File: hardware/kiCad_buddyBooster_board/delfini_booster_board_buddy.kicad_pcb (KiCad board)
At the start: 2 copper layers, 150 parts, among them J1 Screw_Terminal_1x04, J2 Screw_Terminal_1x04, J3 Screw_Terminal_1x04, J4 Screw_Terminal_1x04, J5 1792229, J6 1792229, J7 Screw_Terminal_1x04, J8 1792229, J9 1792229, P1 CONN_01X03, P11 CONN_01X03, P12 CONN_01X03, P13 CONN_01X03, P14 CONN_01X02, P15 CONN_01X03, P16 CONN_01X02, P17 CONN_01X02, P18 CONN_01X03, P19 CONN_01X03, P2 CONN_01X05, P20 CONN_01X03, P21 CONN_01X03, P22 CONN_01X01, P23 CONN_01X01, P24 CONN_01X01, P25 CONN_01X03, P26 CONN_01X01, P27 CONN_01X01, P28 CONN_01X01, P29 CONN_01X03, P3 CONN_01X05, P30 CONN_01X03, P31 CONN_01X03, P32 CONN_01X01, P33 CONN_01X04, P34 CONN_01X04, P4 CONN_02X10, P5 CONN_02X10, P6 CONN_02X10, P7 CONN_02X10, P8 CONN_01X03, P9 CONN_01X03, Q1 2N7002, Q2 2N7002, Q3 2N7002, Q4 2N7002, Q5 IRF9540N, Q6 IRF9540N, Q7 2N7002, U1 TMP275, U2 T90-Relay, U3 tps2112a, U4 LM7812, U5 R-783.3-1.0, U6 T90-Relay, U7 TXB0104

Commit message: -pcb- started routing
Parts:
- moved C20 10.1 mm to (99.1, 95.6), turned to 0 degrees
- moved U1 8.25 mm to (126.4, 103.4), turned to 90 degrees
- moved P18 4.45 mm to (92.2, 108.4)
- moved Q2 4.07 mm to (104.2, 96.4)
- moved R38 3.42 mm to (118.8, 109.1)
- moved Q4 3.42 mm to (111.2, 106.5)
- moved R34 3.24 mm to (104.2, 103.4)
- moved R28 3.24 mm to (99.8, 103.4)
- moved C19 3.24 mm to (99.1, 97.0)
- moved Q7 3.24 mm to (102.9, 106.5)
- moved R37 3.24 mm to (113.7, 109.1)
- moved U3 3.24 mm to (101.0, 100.8)
- moved C29 3.24 mm to (103.6, 109.1)
- moved R27 3.24 mm to (99.8, 104.9)
- moved R29 3.24 mm to (108.8, 98.3)
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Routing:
- net /BAT_PWR_IN: track 0.00 -> 109.1 mm
- net /UART_SABER_TX: track 0.00 -> 106.7 mm, vias 0 -> 2
- net /ULTA1_PULSE_BACK: track 0.00 -> 50.6 mm
- net +5V: track 0.00 -> 50.4 mm
- net /E_BRAKE_IN: track 0.00 -> 50.0 mm
- net /ULTRA0_TRIG_OUT: track 0.00 -> 48.9 mm
- net /ULTRA1_TRIG_OUT: track 0.00 -> 46.3 mm
- net /ULTA0_PULSE_BACK: track 0.00 -> 46.1 mm
- net /MOTOR_BRAKE_EN_N: track 0.00 -> 38.6 mm
- net Net-(Q4-Pad3): track 0.00 -> 37.7 mm
- net Net-(J3-Pad1): track 0.00 -> 23.7 mm
- net Net-(J1-Pad1): track 0.00 -> 13.6 mm
- net Net-(J3-Pad3): track 0.00 -> 11.9 mm
- net /RELAY_COIL: track 0.00 -> 11.7 mm
- net Net-(C21-Pad1): track 0.00 -> 8.81 mm
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- added copper zone on F.Cu, net /BAT_PWR_IN
- added copper zone on F.Cu, net /BAT_PWR_OUT
- added copper zone on F.Cu, net Net-(J6-Pad1)
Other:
- net class 5V added: clearance 0.2, trace_width 1.016, via_dia 0.8, via_drill 0.4

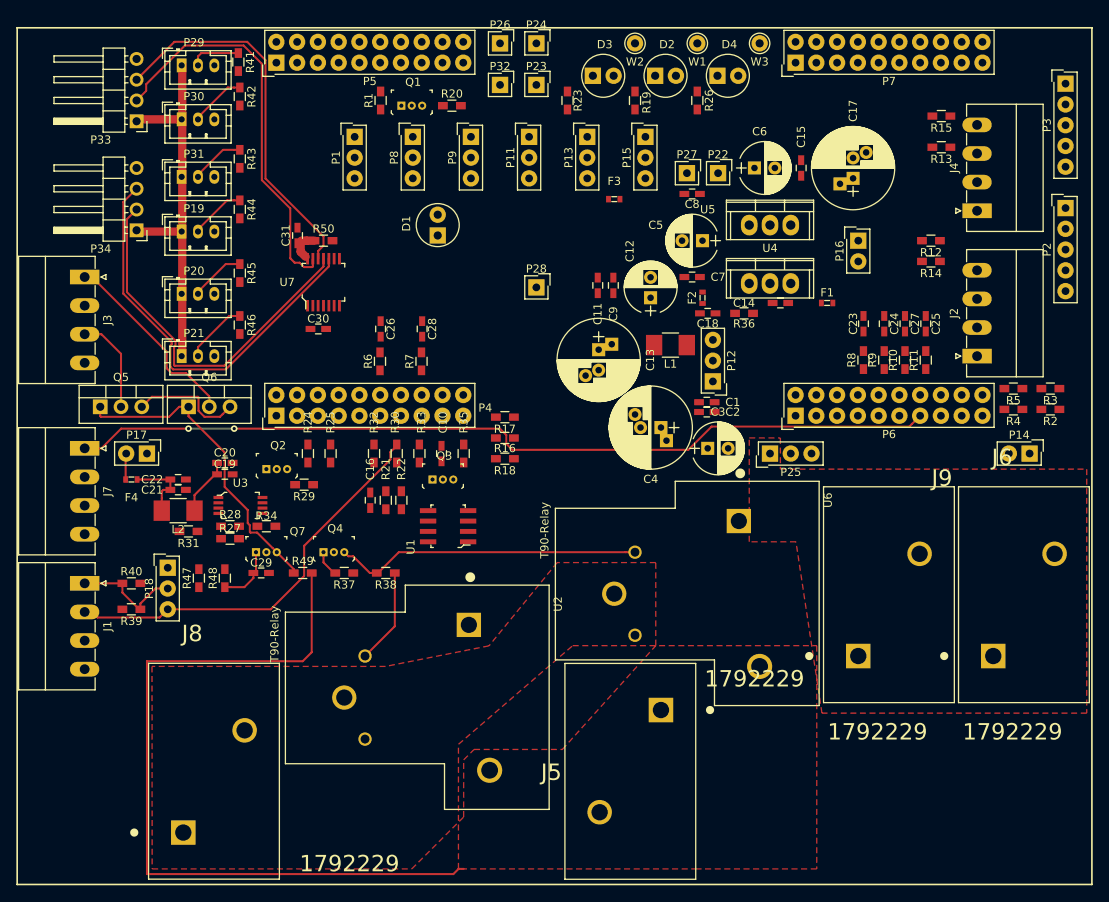
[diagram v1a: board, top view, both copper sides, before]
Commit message: -PCB- Moved Regulators around -PCB- Moved ADC inputs around -Swapped pins around, by grouping
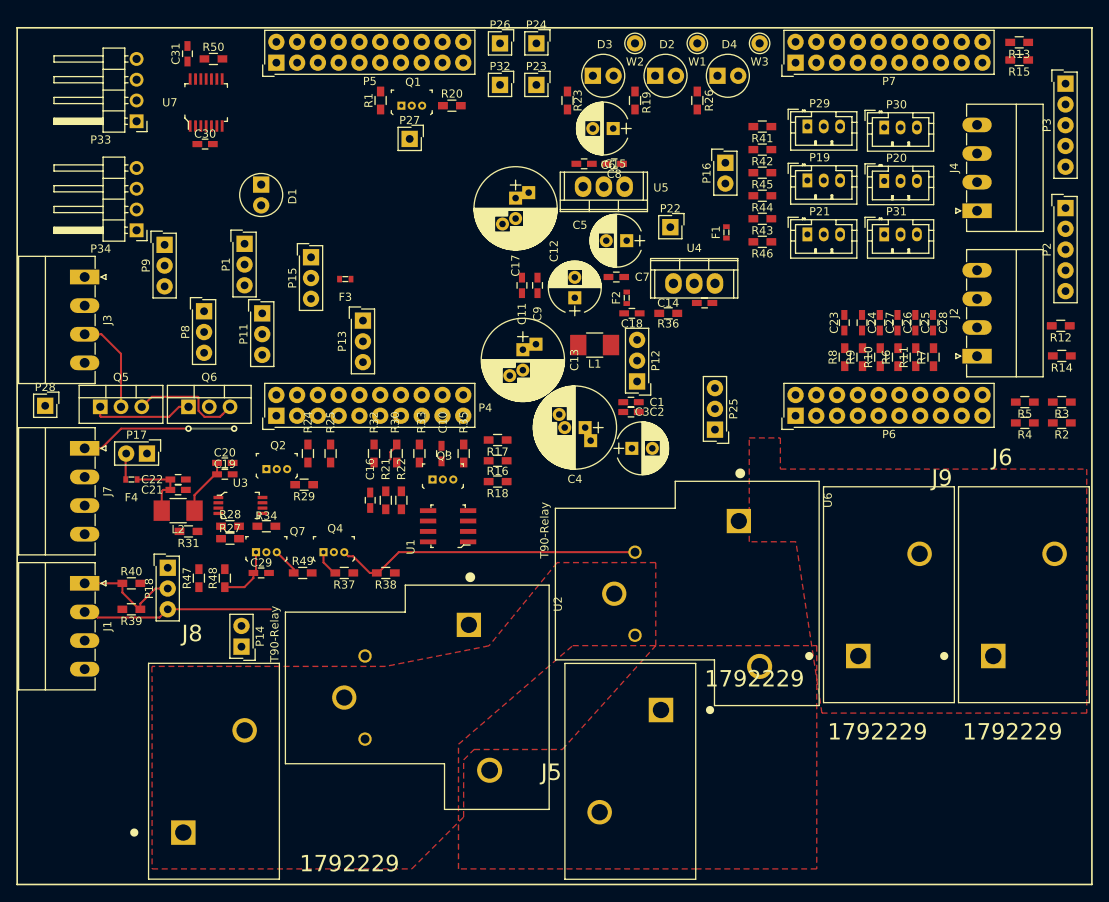
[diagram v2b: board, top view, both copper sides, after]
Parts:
- moved P14 99.2 mm to (101.2, 118.1), turned to 180 degrees
- moved P20 87.0 mm to (179.8, 61.1)
- moved P31 86.2 mm to (179.8, 67.7)
- moved P30 85.9 mm to (179.8, 54.6)
- moved P21 78.0 mm to (170.4, 67.7)
- moved P29 76.9 mm to (170.4, 54.5)
- moved P19 76.8 mm to (170.4, 61.1)
- moved R45 65.1 mm to (164.9, 60.1), turned to 180 degrees
- moved R46 64.7 mm to (164.9, 68.6), turned to 180 degrees
- moved R41 64.6 mm to (164.9, 54.5), turned to 180 degrees
- moved R43 64.3 mm to (164.9, 65.8), turned to 180 degrees
- moved R42 64.2 mm to (164.9, 57.3), turned to 180 degrees
- moved R44 63.9 mm to (164.9, 62.9), turned to 180 degrees
- moved R6 63.4 mm to (181.5, 82.7)
- moved C26 63.2 mm to (181.4, 78.5)
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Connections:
- net /ULTA0_PULSE_BACK renamed /ULTRA0_PULSE_BACK
- net /ULTA1_PULSE_BACK renamed /ULTRA1_PULSE_BACK
- P5 pad 11: Net-(P5-Pad11) -> /ULTRA1_PULSE_BACK_BUFFD
- P5 pad 9: Net-(P5-Pad9) -> /ULTRA0_PULSE_BACK_BUFFD
- P7 pad 1: /ULTA0_PULSE_BACK_BUFFD -> Net-(P7-Pad1)
- P7 pad 3: /ULTA1_PULSE_BACK_BUFFD -> Net-(P7-Pad3)
- R10 pad 1: Net-(P6-Pad16) -> Net-(P6-Pad10)
- R10 pad 2: /ADC4_IN_C2000 -> /ADC2_IN_C2000
- R11 pad 1: Net-(P6-Pad18) -> Net-(P6-Pad14)
- R11 pad 2: /ADC2_IN_C2000 -> /ADC4_IN_C2000
- R6 pad 1: Net-(P4-Pad12) -> Net-(P6-Pad12)
- R7 pad 1: Net-(P4-Pad16) -> Net-(P6-Pad16)
- R8 pad 1: Net-(P6-Pad8) -> Net-(P6-Pad6)
- R9 pad 1: Net-(P6-Pad14) -> Net-(P6-Pad8)
- U7 pad 3: /ULTA0_PULSE_BACK_BUFFD -> /ULTRA0_PULSE_BACK_BUFFD
- U7 pad 5: /ULTA1_PULSE_BACK_BUFFD -> /ULTRA1_PULSE_BACK_BUFFD
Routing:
- net /BAT_PWR_IN: track 109.1 -> 13.8 mm
- net /UART_SABER_TX: track 106.7 -> 19.4 mm
- net /ULTRA1_PULSE_BACK: track 50.6 -> 0.00 mm
- net +5V: track 50.4 -> 0.00 mm
- net /ULTRA0_TRIG_OUT: track 48.9 -> 0.00 mm
- net /ULTRA1_TRIG_OUT: track 46.3 -> 0.00 mm
- net /ULTRA0_PULSE_BACK: track 46.1 -> 0.00 mm
- net /E_BRAKE_IN: track 50.0 -> 25.6 mm
- net Net-(J3-Pad1): track 23.7 -> 0.90 mm
- net /MOTOR_BRAKE_EN_N: track 38.6 -> 15.9 mm
- net /RELAY_COIL: track 11.7 -> 0.00 mm
- net /ADC5_OUTPUT: track 7.79 -> 0.00 mm
- net /ADC1_OUTPUT: track 6.87 -> 0.00 mm
- net /ADC3_OUTPUT: track 6.84 -> 0.00 mm
- net /ADC4_OUTPUT: track 6.77 -> 0.00 mm
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
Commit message: -PCB- End of night commit. Minor tweaks
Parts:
- moved R1 24.4 mm to (96.5, 62.3)
- moved R18 7.93 mm to (133.4, 90.0)
- moved R40 7.01 mm to (88.3, 103.4)
- moved C25 4.34 mm to (179.2, 78.5)
- moved C27 4.34 mm to (183.6, 78.5)
- moved L2 3.81 mm to (93.4, 97.6)
- moved C10 3.01 mm to (122.6, 94.5)
- moved C16 2.62 mm to (114.4, 100.8)
- moved R21 2.62 mm to (116.3, 100.8)
- moved R22 2.62 mm to (118.2, 100.8)
- moved C21 2.62 mm to (92.8, 101.4)
- moved C22 2.62 mm to (92.8, 100.2)
- moved Q3 2.62 mm to (122.0, 98.3)
- moved R30 2.54 mm to (117.6, 94.5)
- moved R32 2.54 mm to (114.8, 94.5)
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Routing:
- net /E_BRAKE_IN: track 25.6 -> 2.00 mm
- net /UART_SABER_TX: track 19.4 -> 0.00 mm, vias 2 -> 0
- net Net-(J1-Pad1): track 13.6 -> 0.15 mm
- net Net-(J3-Pad3): track 11.9 -> 0.00 mm
- net Net-(C21-Pad1): track 8.81 -> 0.00 mm
- net Net-(C29-Pad1): track 7.25 -> 0.45 mm
- net Net-(C19-Pad1): track 7.12 -> 1.62 mm
- net /TMP275_ALERT_OD: track 0.00 -> 4.85 mm
- net Net-(P6-Pad6): track 0.00 -> 3.91 mm
- net Net-(P6-Pad16): track 0.00 -> 3.90 mm
- net Net-(P6-Pad8): track 0.00 -> 3.76 mm
- net Net-(P6-Pad14): track 0.00 -> 3.75 mm
- net Net-(P6-Pad10): track 0.00 -> 3.61 mm
- net Net-(P6-Pad12): track 0.00 -> 3.59 mm
- net /MOTOR_BRAKE_EN_N: track 15.9 -> 12.5 mm
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- added copper zone on B.Cu, net GND

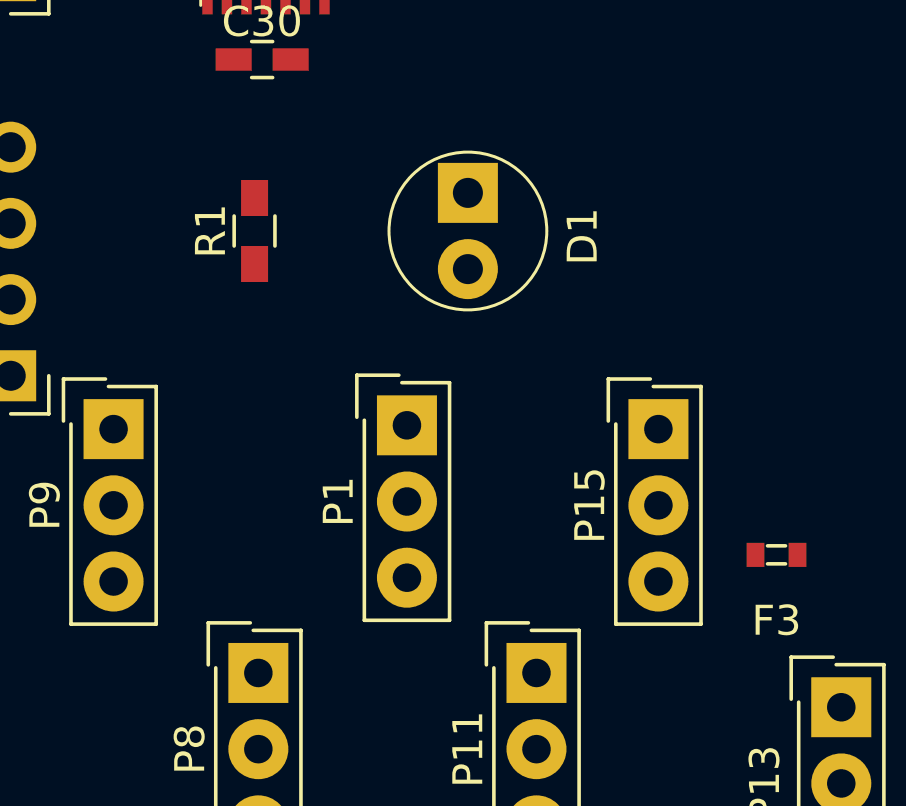
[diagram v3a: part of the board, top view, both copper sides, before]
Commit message: -updated led debug_en circuit
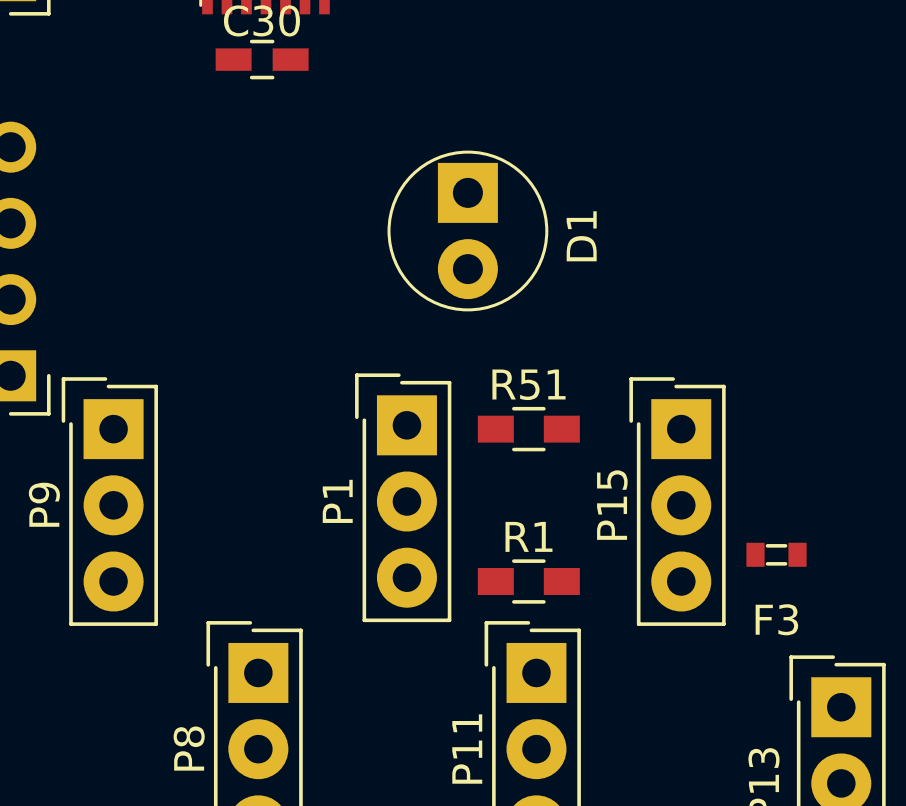
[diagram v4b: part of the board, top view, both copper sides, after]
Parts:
- added R51: R, Resistors_SMD:R_0603_HandSoldering, F.Cu at (105.6, 68.9)
- moved R1 14.8 mm to (105.6, 74.0), turned to 0 degrees
- moved P15 0.76 mm to (110.7, 68.9)
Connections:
- P1 pad 1: Net-(P1-Pad1) -> Net-(D1-Pad2)
- P1 pad 2: /TEST_EN_N -> GND
- P1 pad 3: Net-(D1-Pad2) -> /TEST_EN_N
